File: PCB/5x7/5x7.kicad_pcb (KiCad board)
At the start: 2 copper layers, 11 x 13 mm, 49 parts, among them J1 Conn_01x03, J2 Conn_01x03

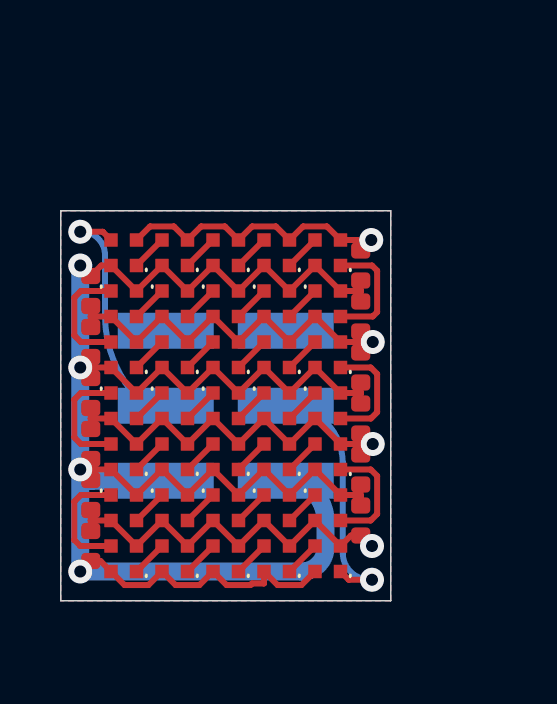
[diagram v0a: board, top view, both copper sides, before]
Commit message: Reworked for orientation, and ordered
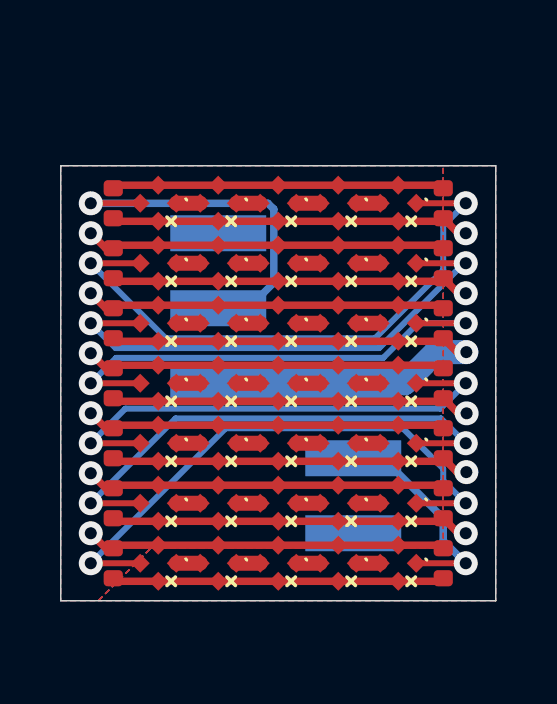
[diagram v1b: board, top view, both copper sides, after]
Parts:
- added C13: 330nF, RevK:C_0402, F.Cu at (101.8, 86.8)
- added C14: 330nF, RevK:C_0402, F.Cu at (112.8, 86.8)
- moved D10 9.25 mm to (111.2, 88.8), turned to -135 degrees
- moved D20 9.18 mm to (111.2, 92.8), turned to -135 degrees
- moved D30 9.15 mm to (111.2, 96.8), turned to -135 degrees
- moved D6 5.81 mm to (103.2, 88.8), turned to -135 degrees
- moved D16 5.70 mm to (103.2, 92.8), turned to -135 degrees
- moved D26 5.65 mm to (103.2, 96.8), turned to -135 degrees
- moved D9 5.61 mm to (109.2, 88.8), turned to -135 degrees
- moved D19 5.50 mm to (109.2, 92.8), turned to -135 degrees
- moved D29 5.45 mm to (109.2, 96.8), turned to -135 degrees
- moved J1 3.69 mm to (105.2, 90.2)
- moved C7 3.10 mm to (112.8, 98.8), turned to 90 degrees
- moved C12 2.97 mm to (112.8, 96.8)
- moved D5 2.87 mm to (111.2, 86.8), turned to -135 degrees
- moved C11 2.87 mm to (112.8, 94.8), turned to 90 degrees
- moved J2 2.85 mm to (109.8, 95.2), turned to -90 degrees
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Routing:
- net GND: track 50.7 -> 81.3 mm, vias 4 -> 6
- net Net-(D5-O): track 3.96 -> 23.2 mm, vias 0 -> 2
- net Net-(D30-O): track 3.90 -> 22.6 mm, vias 0 -> 2
- net Net-(D25-O): track 3.89 -> 21.0 mm, vias 0 -> 2
- net Net-(D10-O): track 3.89 -> 21.0 mm, vias 0 -> 2
- net Net-(D20-O): track 3.89 -> 20.3 mm, vias 0 -> 2
- net Net-(D15-O): track 3.90 -> 20.3 mm, vias 0 -> 2
- net VDD: track 75.7 -> 90.1 mm, vias 4 -> 6
- net Net-(D1-I): track 8.35 -> 14.3 mm
- net Net-(D35-O): track 8.37 -> 9.11 mm
- added copper zone on B.Cu, net VDD
- added copper zone on F.Cu, net VDD
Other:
- board size 11 x 13 mm -> 14.5 x 14.5 mm

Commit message: Date
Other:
- board text added: "${CURRENT_DATE}"

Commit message: Indent
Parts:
- moved C6 13.3 mm to (112.4, 90.8)
- moved C4 12.2 mm to (112.4, 88.8)
- moved C7 12.2 mm to (102.1, 92.8)
- moved C13 12.0 mm to (102.1, 98.8)
- moved C14 12.0 mm to (112.4, 98.8)
- moved C2 11.4 mm to (112.4, 86.8)
- moved C9 11.4 mm to (102.1, 94.8)
- moved C11 10.8 mm to (102.1, 96.8)
- moved C5 6.01 mm to (102.1, 90.8)
- moved C3 4.02 mm to (102.1, 88.8)
- moved C8 4.02 mm to (112.4, 92.8)
- moved C1 2.03 mm to (102.1, 86.8)
- moved C10 2.03 mm to (112.4, 94.8)
- moved C12 0.35 mm to (112.4, 96.8)

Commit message: Some tracks
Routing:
- net (no net): track 0.00 -> 156.4 mm
- net VDD: track 90.1 -> 0.00 mm, vias 6 -> 0
- net GND: track 81.3 -> 0.00 mm, vias 6 -> 0
- net Net-(D5-O): track 23.2 -> 0.00 mm, vias 2 -> 0
- net Net-(D30-O): track 22.6 -> 0.00 mm, vias 2 -> 0
- net Net-(D25-O): track 21.0 -> 0.00 mm, vias 2 -> 0
- net Net-(D10-O): track 21.0 -> 0.00 mm, vias 2 -> 0
- net Net-(D20-O): track 20.3 -> 0.00 mm, vias 2 -> 0
- net Net-(D15-O): track 20.3 -> 0.00 mm, vias 2 -> 0
- net Net-(D1-I): track 14.3 -> 0.00 mm, vias 1 -> 0
- net Net-(D35-O): track 9.11 -> 0.00 mm, vias 1 -> 0
- net Net-(D8-O): track 0.80 -> 0.00 mm
- net Net-(D7-O): track 0.80 -> 0.00 mm
- net Net-(D6-O): track 0.80 -> 0.00 mm
- net Net-(D4-O): track 0.80 -> 0.00 mm
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
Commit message: power
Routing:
- net (no net): track 156.4 -> 984.7 mm

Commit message: Tracking
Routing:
- net (no net): track 984.7 -> 1908.3 mm, vias 0 -> 80

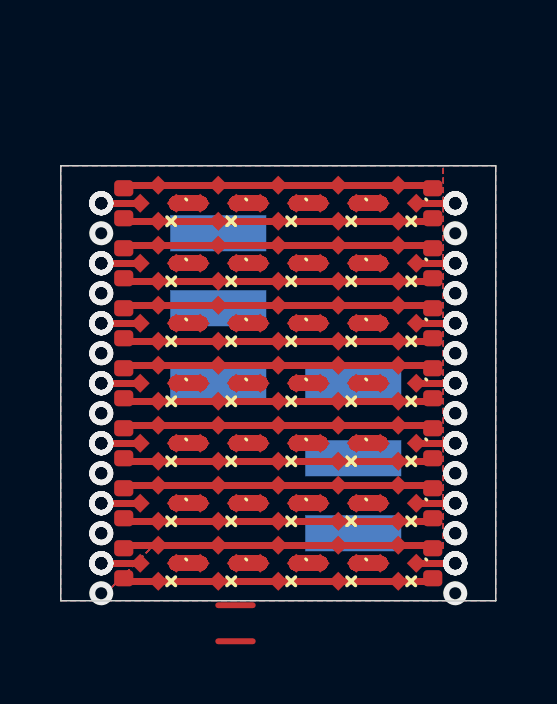
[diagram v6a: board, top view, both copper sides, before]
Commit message: Works - would be nice to have a way to delete the created old entries...
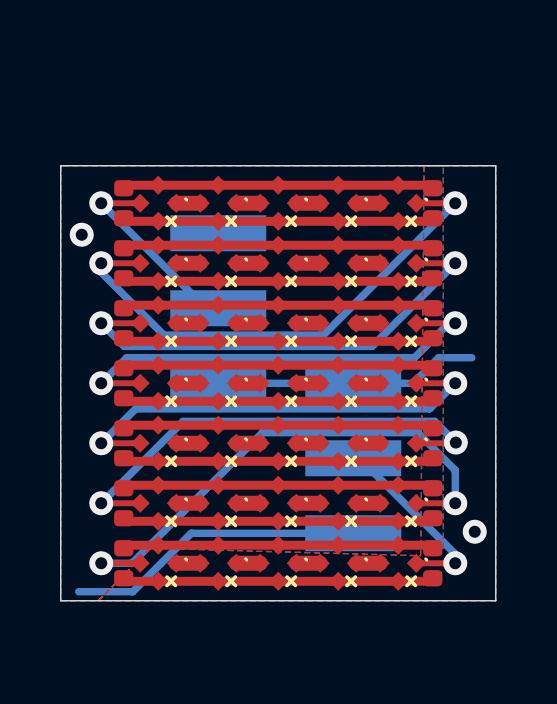
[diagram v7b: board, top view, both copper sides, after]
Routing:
- net (no net): track 1908.3 -> 0.00 mm, vias 80 -> 0
- net GND: track 0.00 -> 82.1 mm, vias 0 -> 1
- net VDD: track 0.00 -> 80.9 mm, vias 0 -> 1
- net Net-(D30-O): track 0.00 -> 17.8 mm, vias 0 -> 2
- net Net-(D5-O): track 0.00 -> 17.4 mm, vias 0 -> 2
- net Net-(D25-O): track 0.00 -> 15.9 mm, vias 0 -> 2
- net Net-(D10-O): track 0.00 -> 15.9 mm, vias 0 -> 2
- net Net-(D15-O): track 0.00 -> 15.2 mm, vias 0 -> 2
- net Net-(D20-O): track 0.00 -> 15.2 mm, vias 0 -> 2
- net Net-(D1-I): track 0.00 -> 6.65 mm, vias 0 -> 1
- net Net-(D35-O): track 0.00 -> 6.33 mm, vias 0 -> 1
- net Net-(D8-O): track 0.00 -> 0.80 mm
- net Net-(D7-O): track 0.00 -> 0.80 mm
- net Net-(D6-O): track 0.00 -> 0.80 mm
- net Net-(D4-O): track 0.00 -> 0.80 mm
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
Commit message: New layout
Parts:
- removed C11, C12, C13, C14: 330nF, RevK:C_0402
- moved C2 16.1 mm to (101.0, 98.2), turned to 0 degrees
- moved C4 13.3 mm to (103.0, 98.2), turned to 0 degrees
- moved C9 12.9 mm to (109.0, 83.8), turned to 0 degrees
- moved D5 12.0 mm to (101.0, 93.0), turned to 135 degrees
- moved D29 11.8 mm to (109.0, 85.0), turned to 135 degrees
- moved D31 11.3 mm to (109.0, 89.0), turned to 135 degrees
- moved C6 10.5 mm to (105.0, 98.2), turned to 0 degrees
- moved C7 10.2 mm to (107.0, 83.8), turned to 0 degrees
- moved D30 10.0 mm to (109.0, 87.0), turned to 135 degrees
- moved D22 9.91 mm to (107.0, 85.0), turned to 135 degrees
- moved D4 9.28 mm to (101.0, 91.0), turned to 135 degrees
- moved D7 9.28 mm to (101.0, 97.0), turned to 135 degrees
- moved D14 8.84 mm to (103.0, 97.0), turned to 135 degrees
- moved D32 8.61 mm to (109.0, 91.0), turned to 135 degrees
- moved D15 8.49 mm to (105.0, 85.0), turned to 135 degrees
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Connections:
- net VDD renamed VCC
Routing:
- net Net-(D7-O): track 0.80 -> 20.5 mm, vias 0 -> 2
- net Net-(D28-O): track 0.80 -> 20.4 mm, vias 0 -> 2
- net Net-(D21-O): track 0.80 -> 19.2 mm, vias 0 -> 2
- net Net-(D14-O): track 0.80 -> 19.2 mm, vias 0 -> 2
- net Net-(D30-O): track 17.8 -> 0.80 mm, vias 2 -> 0
- net Net-(D5-O): track 17.4 -> 0.80 mm, vias 2 -> 0
- net Net-(D25-O): track 15.9 -> 0.80 mm, vias 2 -> 0
- net Net-(D10-O): track 15.9 -> 0.80 mm, vias 2 -> 0
- net Net-(D15-O): track 15.2 -> 0.80 mm, vias 2 -> 0
- net Net-(D20-O): track 15.2 -> 0.80 mm, vias 2 -> 0
- net GND: track 82.1 -> 71.5 mm, vias 1 -> 4
- net VCC: track 80.9 -> 71.5 mm, vias 1 -> 4
- net Net-(D35-O): track 6.33 -> 10.9 mm
- net Net-(D1-I): track 6.65 -> 10.8 mm
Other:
- board size 14.5 x 14.5 mm -> 10 x 18 mm
